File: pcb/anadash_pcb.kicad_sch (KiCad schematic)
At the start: 17 parts, among them J1 ${FAMILY}, J2 ${FAMILY}, J3 ${FAMILY}, J4 ${FAMILY}, J5 ${FAMILY}, J6 ${FAMILY}, J7 ${FAMILY}, J8 ${FAMILY}

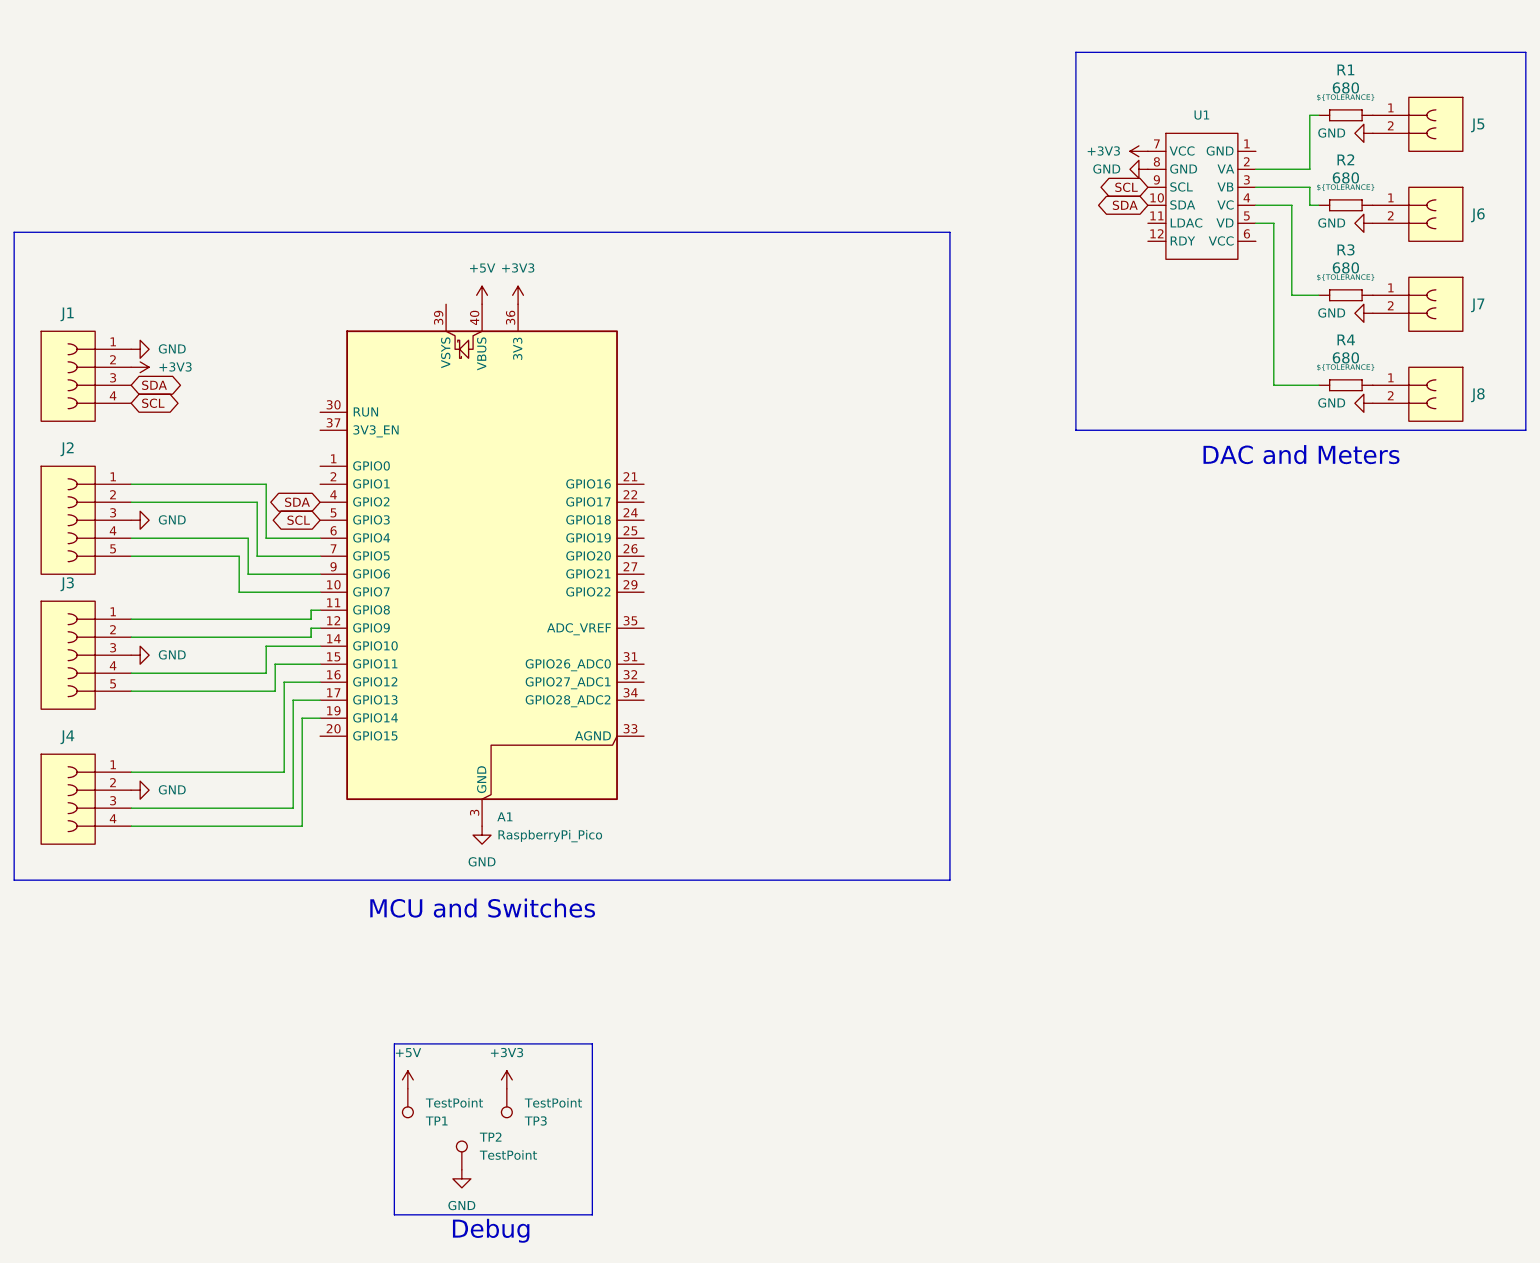
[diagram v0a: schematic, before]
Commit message: Ground should point downwards so i fixed that
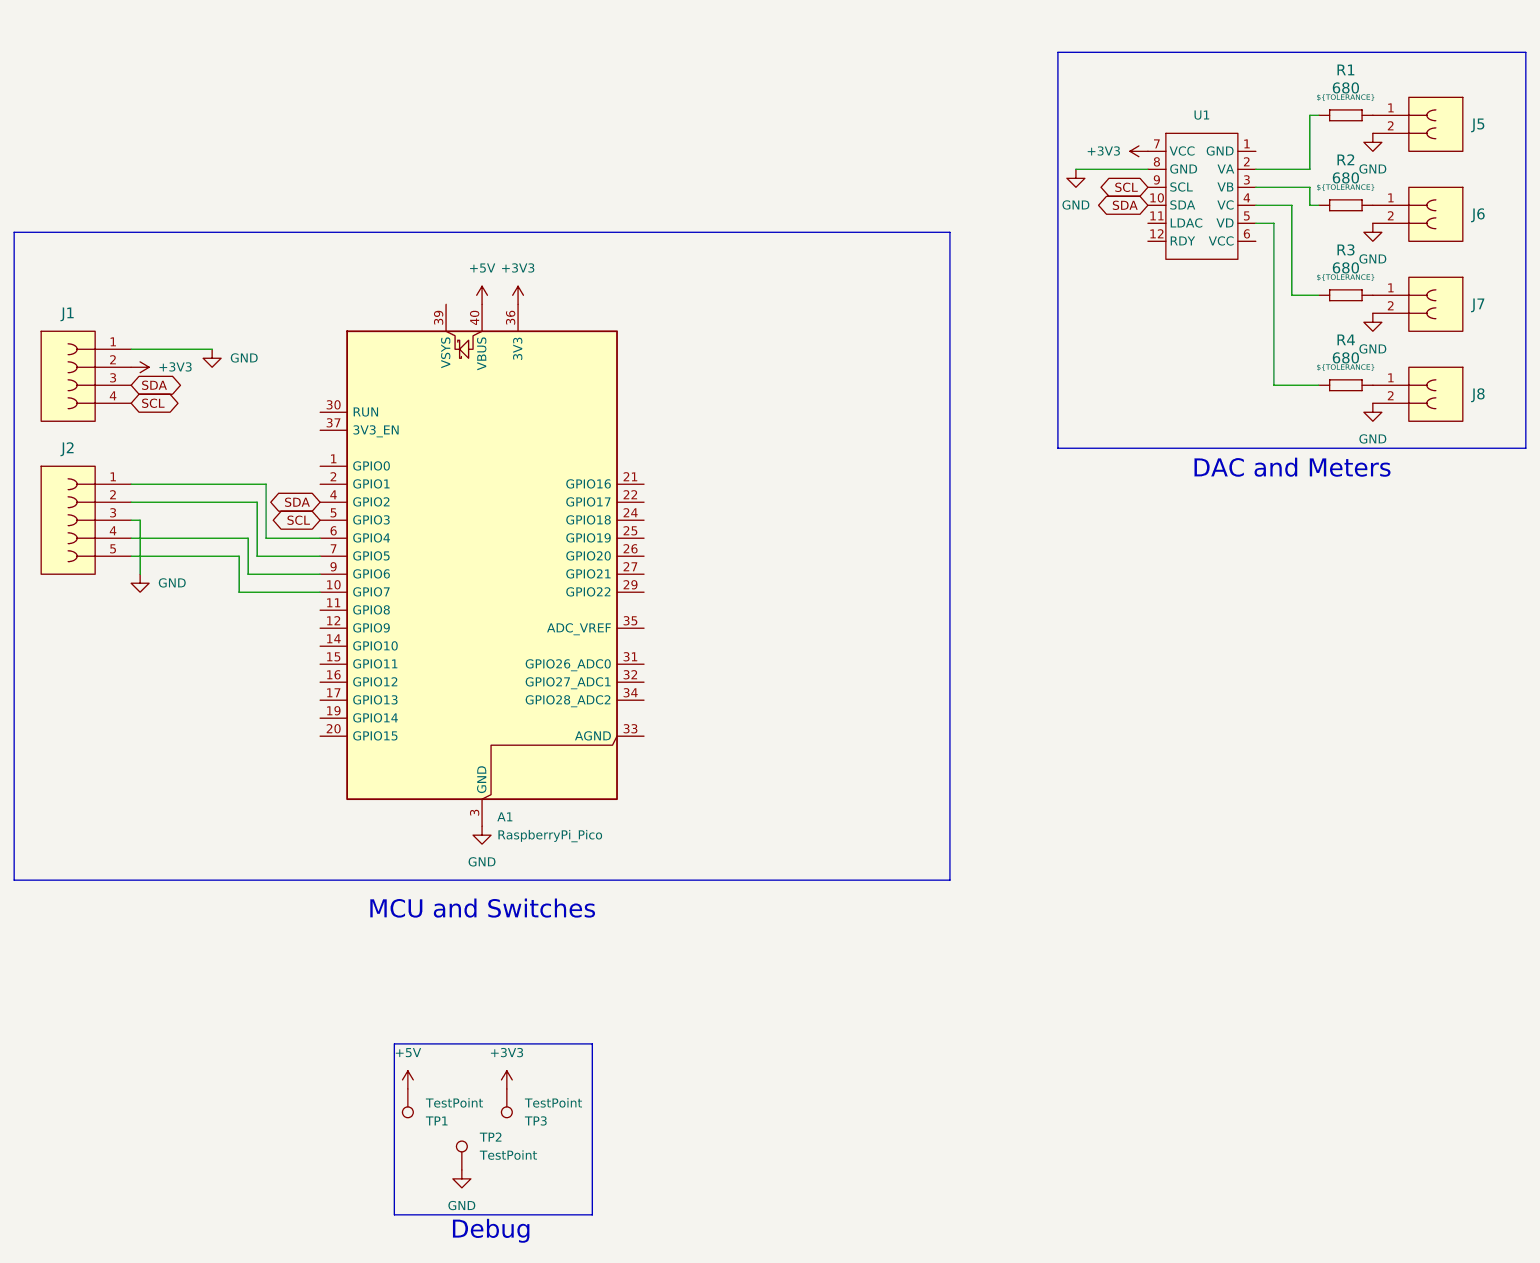
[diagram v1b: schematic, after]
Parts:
- removed J3: ${FAMILY}, symbol Connectors:Connector 5 Female
- removed J4: ${FAMILY}, symbol Connectors:Connector 4 Female
- J1: footprint (none) -> Connector_JST:JST_XH_B4B-XH-A_1x04_P2.50mm_Vertical
- J2: footprint (none) -> Connector_JST:JST_XH_B5B-XH-A_1x05_P2.50mm_Vertical
- J5, J6, J7, J8: footprint (none) -> Connector_JST:JST_XH_B2B-XH-A_1x02_P2.50mm_Vertical
- TP1, TP2, TP3: footprint (none) -> TestPoint:TestPoint_Pad_D2.5mm

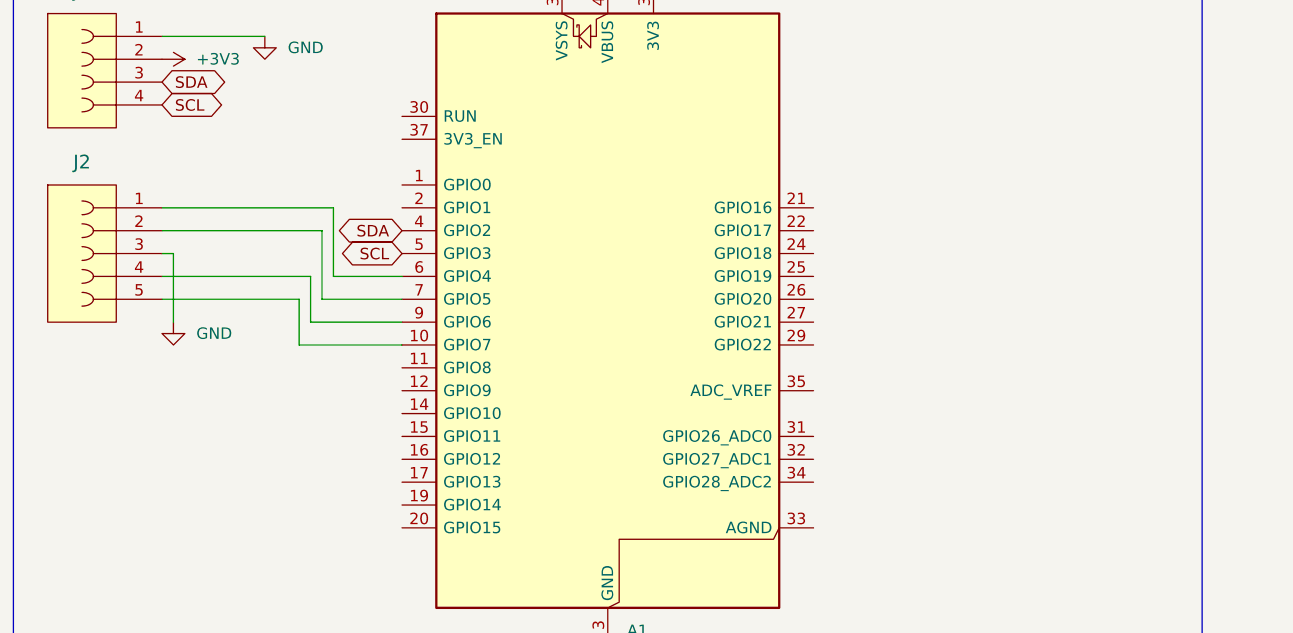
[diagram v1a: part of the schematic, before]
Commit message: Wire up the schematic for the switches
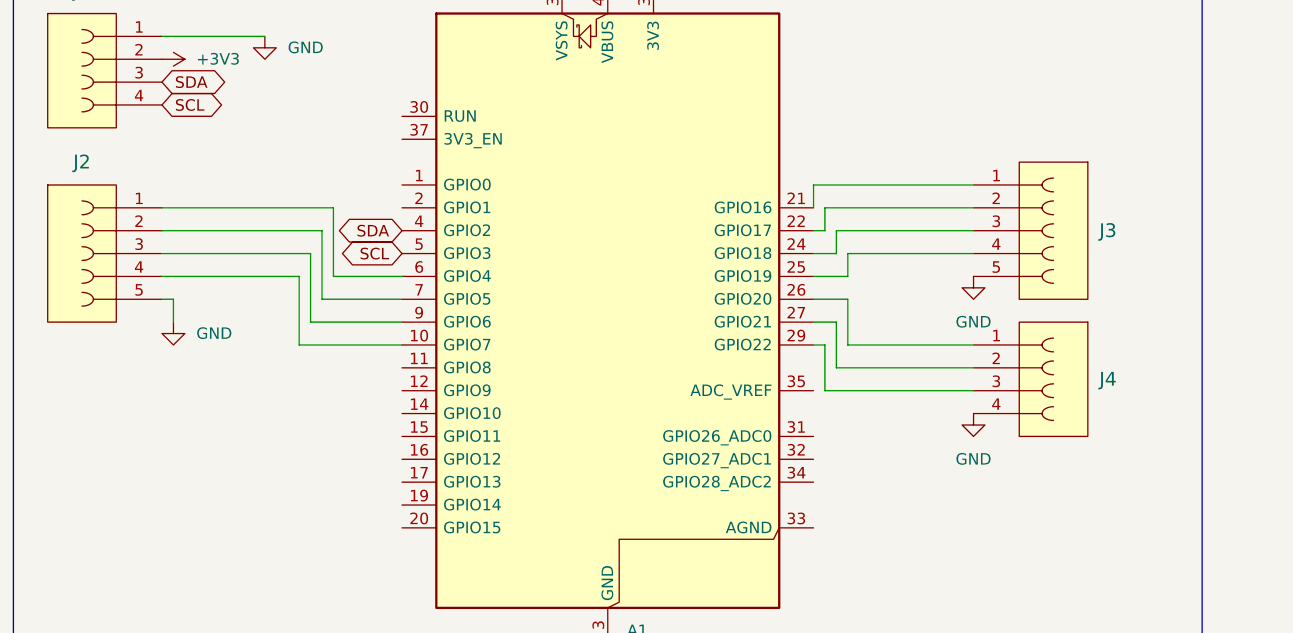
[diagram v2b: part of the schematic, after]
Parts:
- added J3: ${FAMILY}, Connector_JST:JST_XH_B5B-XH-A_1x05_P2.50mm_Vertical, symbol Connectors:Connector 5 Female
- added J4: ${FAMILY}, Connector_JST:JST_XH_B4B-XH-A_1x04_P2.50mm_Vertical, symbol Connectors:Connector 4 Female
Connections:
- net GND: now also J2.5, J3.5, J4.4; no longer J2.3
- net at A1.10 (GPIO7): now also J2.4; no longer J2.5
- net at A1.21 (GPIO16): now also J3.1
- net at A1.22 (GPIO17): now also J3.2
- net at A1.24 (GPIO18): now also J3.3
- net at A1.25 (GPIO19): now also J3.4
- net at A1.26 (GPIO20): now also J4.1
- net at A1.27 (GPIO21): now also J4.2
- net at A1.29 (GPIO22): now also J4.3
- net at A1.9 (GPIO6): now also J2.3; no longer J2.4

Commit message: Fix the 46 ERC rules
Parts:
- removed J1, J4: ${FAMILY}, Connector_JST:JST_XH_B4B-XH-A_1x04_P2.50mm_Vertical, symbol Connectors:Connector 4 Female
- removed J2, J3: ${FAMILY}, Connector_JST:JST_XH_B5B-XH-A_1x05_P2.50mm_Vertical, symbol Connectors:Connector 5 Female
- removed J5, J6, J7, J8: ${FAMILY}, Connector_JST:JST_XH_B2B-XH-A_1x02_P2.50mm_Vertical, symbol Connectors:Connector 2 Female
- added J?: EncoderConnector, symbol Connector_Generic:Conn_01x04
- added J?: RightKeyConnector, symbol Connector_Generic:Conn_01x05
- added J?: LeftKeyConnector, symbol Connector_Generic:Conn_01x05
- added J?: DisplayConnector, symbol Connector_Generic:Conn_01x04
- added MES? (x4): Ammeter_DC, symbol Device:Ammeter_DC
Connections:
- net +3V3: now also J?.2 (Pin_2)
- net GND: now also J?.1 (Pin_1), J?.4 (Pin_4), J?.5 (Pin_5), J?.5 (Pin_5), MES?.1 (-), MES?.1 (-), MES?.1 (-), MES?.1 (-)
- net SCL: now also J?.4 (Pin_4)
- net SDA: now also J?.3 (Pin_3)
- net at A1.10 (GPIO7): now also J?.4 (Pin_4)
- net at A1.21 (GPIO16): now also J?.1 (Pin_1)
- net at A1.22 (GPIO17): now also J?.2 (Pin_2)
- net at A1.24 (GPIO18): now also J?.3 (Pin_3)
- net at A1.25 (GPIO19): now also J?.4 (Pin_4)
- net at A1.26 (GPIO20): now also J?.1 (Pin_1)
- net at A1.27 (GPIO21): now also J?.2 (Pin_2)
- net at A1.29 (GPIO22): now also J?.3 (Pin_3)
- net at A1.6 (GPIO4): now also J?.1 (Pin_1)
- net at A1.7 (GPIO5): now also J?.2 (Pin_2)
- net at A1.9 (GPIO6): now also J?.3 (Pin_3)
- net at R1.2: now also MES?.2 (+)
- net at R3.2: now also MES?.2 (+)
- net at R2.2: now also MES?.2 (+)
- net at R4.2: now also MES?.2 (+)
- no-connect marks 0 -> 22
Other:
- moved on the sheet: R1, R2, R3, R4
